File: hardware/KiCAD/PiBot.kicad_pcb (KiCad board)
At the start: 2 copper layers, 112 x 87 mm, 179 parts, among them P1 BREAKOUT, P10 BREAKOUT, P11 BREAKOUT, P12 BREAKOUT, P2 CONN_02X05, P3 I2C_EXPANSION, P4 SPI_EXPANSION, P5 Feather-Adaper, P6 BREAKOUT, P7 BREAKOUT, P8 BREAKOUT, P9 BREAKOUT, SW1 SPST, SW2 SW_SPDT, SW3 SW_SPDT, SW4 SW_SPDT, SW5 SW_SPDT, U1 DMG2302U, U10 AH3772, U11 AH3772, U12 AH3772, U13 BH1745NUC, U14 BH1745NUC, U15 L3GD20H, U16 LSM303DLHCTR, U17 N-FET, U2 MKL03ZxxVFK4, U3 N-FET, U4 TPS63060, U5 MC33926PNB, U6 MC33926PNB, U7 Motor, U8 Motor, U9 AH3772

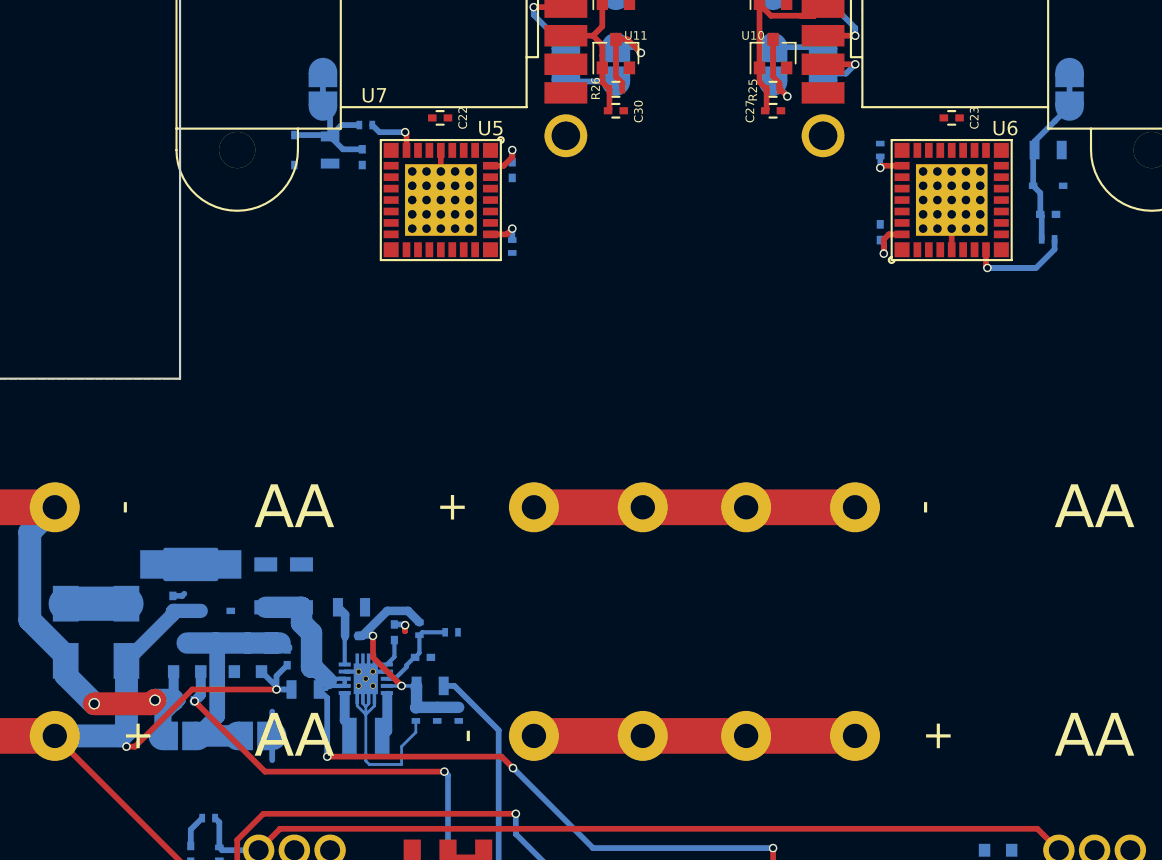
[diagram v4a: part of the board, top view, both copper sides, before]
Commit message: Wire up motor drive power
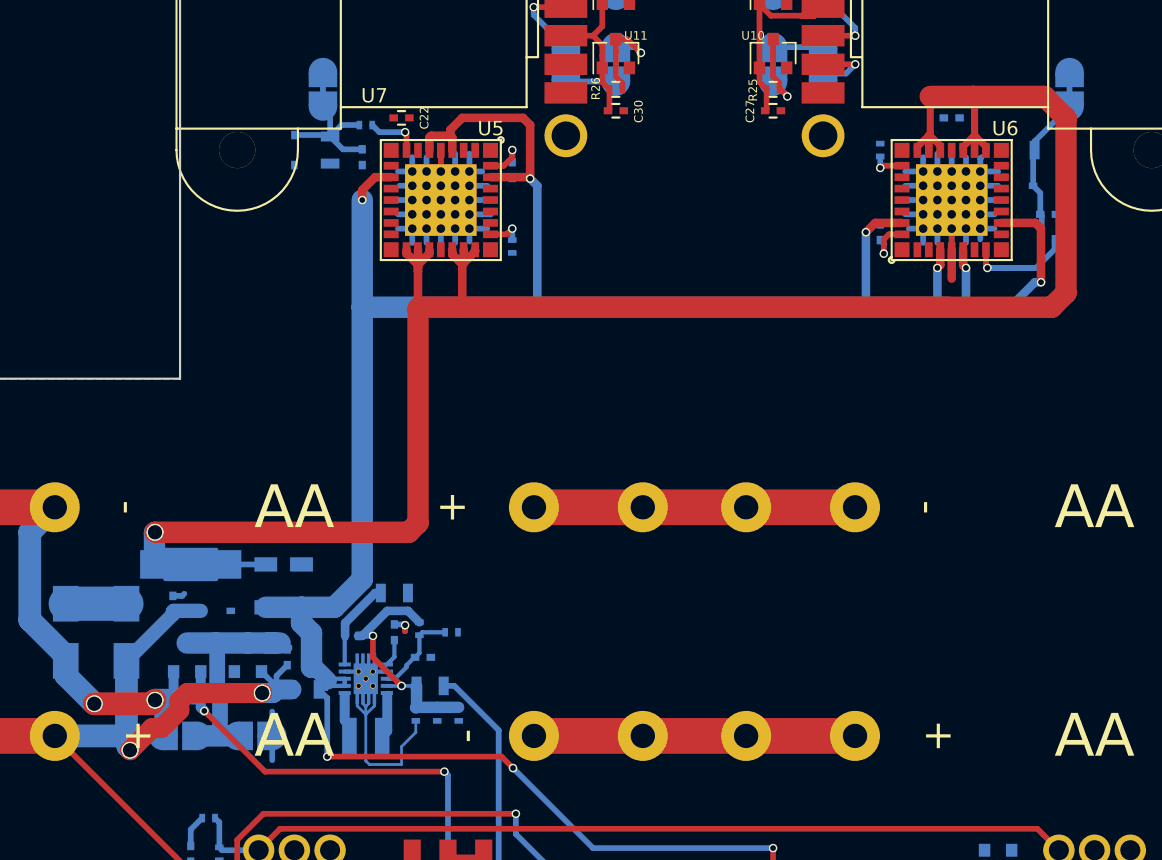
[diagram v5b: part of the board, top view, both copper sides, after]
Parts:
- C23: moved to B.Cu
- moved R12 3.16 mm to (122.0, 150.0)
- moved C22 2.70 mm to (122.5, 116.8)
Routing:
- net +BATT: track 57.2 -> 189.0 mm, vias 4 -> 10
- net GNDPWR: track 0.00 -> 131.5 mm, vias 0 -> 1
- net GND: track 25.9 -> 73.9 mm
- net Net-(R12-Pad2): track 4.22 -> 6.28 mm
- net Net-(C9-Pad2): track 17.5 -> 18.5 mm
- net /power/BATT_V+_TERM: track 78.8 -> 79.4 mm

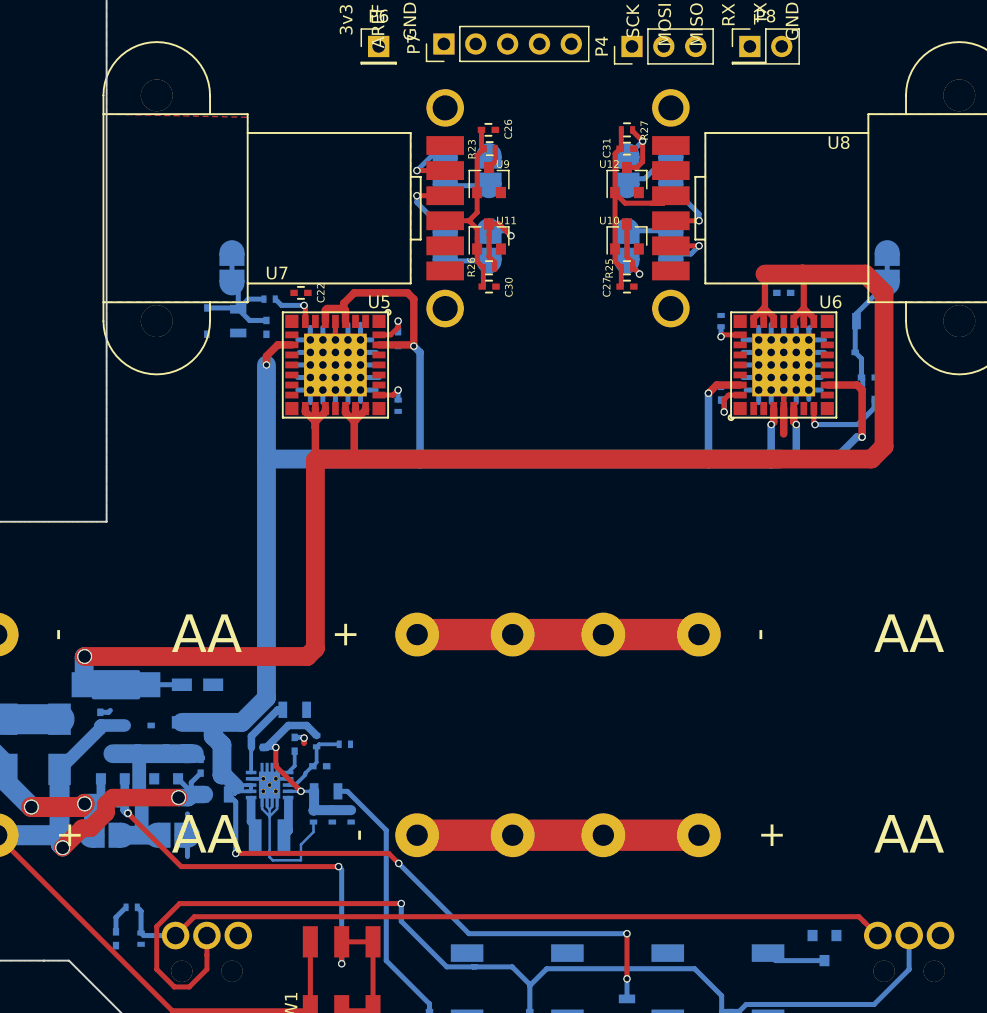
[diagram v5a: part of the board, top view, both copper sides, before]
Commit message: Motor drives wired up
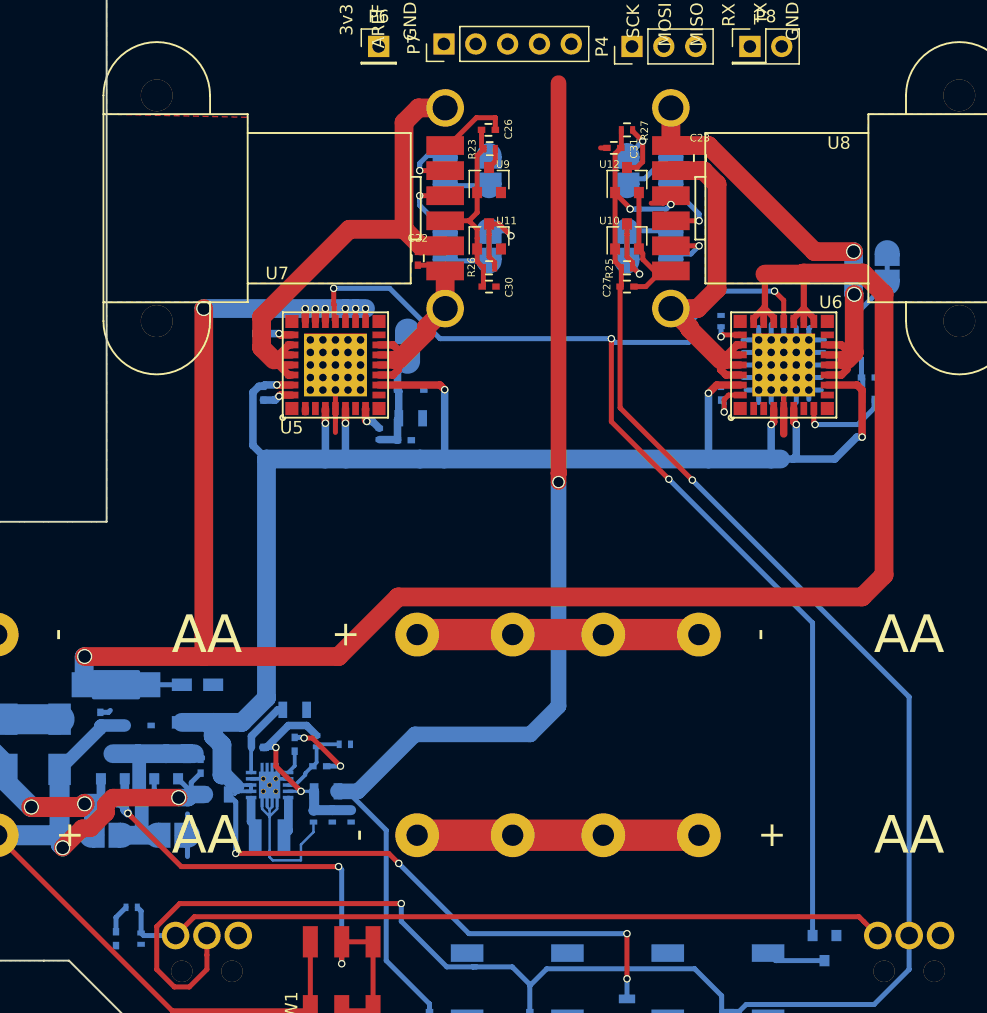
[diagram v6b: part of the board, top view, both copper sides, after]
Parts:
- C23: moved to F.Cu
- moved D11 17.2 mm to (131.2, 124.5), turned to 0 degrees
- moved R17 15.8 mm to (131.2, 126.8), turned to 0 degrees
- moved JP5 15.3 mm to (131.0, 121.0)
- moved C20 14.2 mm to (130.8, 128.5), turned to 0 degrees
- moved R19 13.9 mm to (128.8, 128.0), turned to 270 degrees
- moved C23 12.7 mm to (154.3, 106.0), turned to 270 degrees
- moved R21 12.4 mm to (119.2, 120.0), turned to 180 degrees
- moved C19 11.6 mm to (119.5, 124.8), turned to 270 degrees
- moved C22 9.72 mm to (131.8, 114.0), turned to 90 degrees
- moved C31 1.05 mm to (147.4, 105.2), turned to 180 degrees
- turned U5 to 90 degrees
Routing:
- net ~MotorSF: track 0.00 -> 99.2 mm, vias 0 -> 4
- net +5V: track 21.0 -> 91.2 mm, vias 0 -> 1
- net +3V3: track 119.3 -> 181.6 mm, vias 1 -> 4
- net Net-(C22-Pad2): track 0.00 -> 42.0 mm
- net Net-(C23-Pad1): track 0.00 -> 39.5 mm, vias 0 -> 2
- net Net-(C23-Pad2): track 0.00 -> 31.1 mm
- net GNDPWR: track 131.5 -> 162.3 mm, vias 1 -> 8
- net Net-(C22-Pad1): track 0.00 -> 19.4 mm
- net +BATT: track 189.0 -> 181.0 mm, vias 10 -> 12
- net GND: track 73.9 -> 77.5 mm, vias 1 -> 2
- net Net-(C20-Pad1): track 9.85 -> 8.18 mm
- net Net-(R19-Pad1): track 3.82 -> 2.42 mm
- net Net-(R32-Pad1): track 41.5 -> 42.2 mm
- net Net-(C19-Pad2): track 3.12 -> 2.44 mm

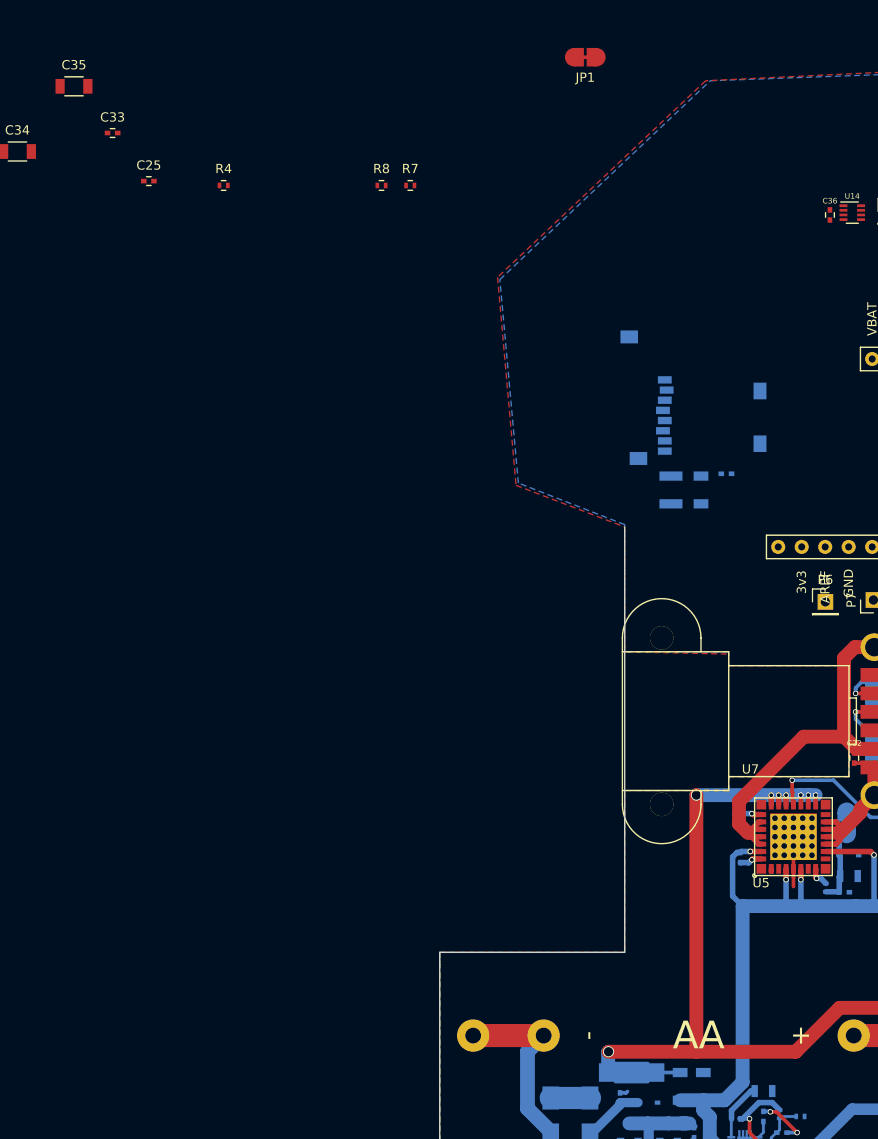
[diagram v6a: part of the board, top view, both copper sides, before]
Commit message: fixing GND_PWR connection
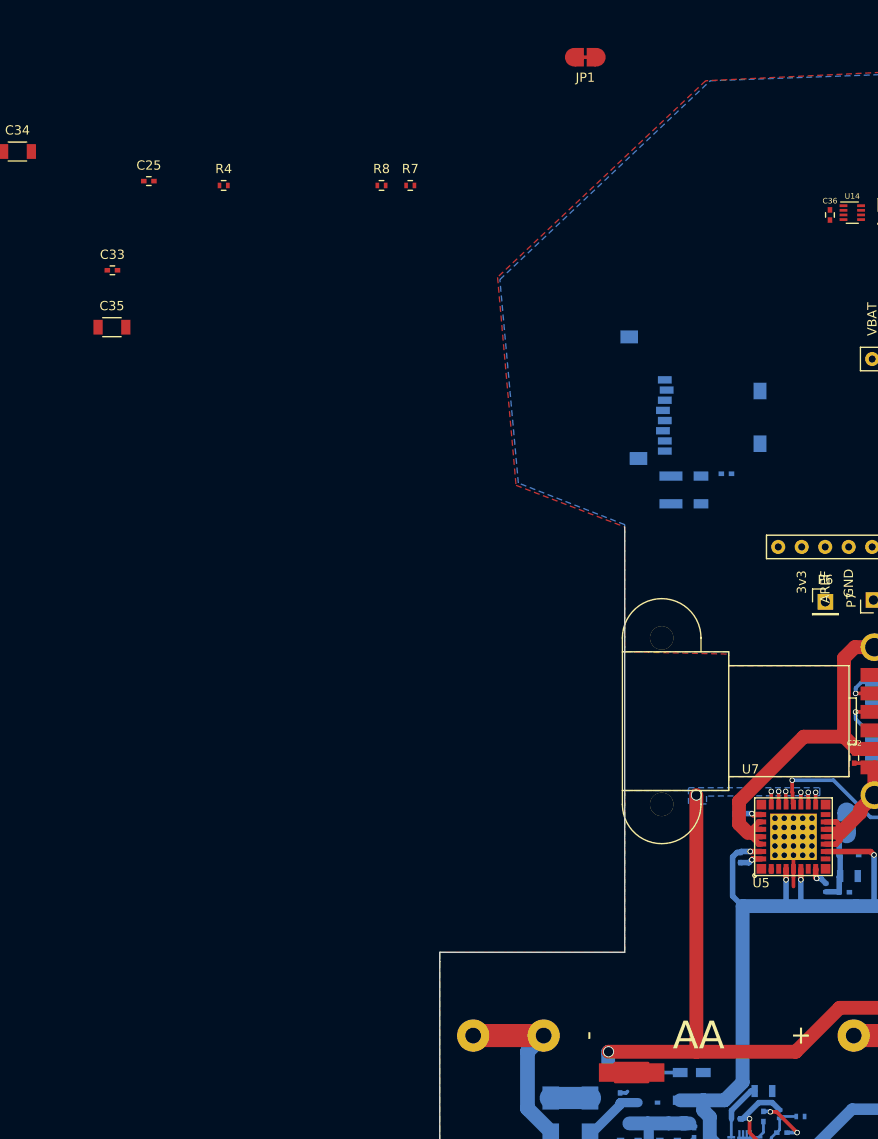
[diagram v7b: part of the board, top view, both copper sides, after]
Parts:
- JP17: moved to F.Cu
- moved C35 26.4 mm to (51.5, 67.4)
- moved C33 14.8 mm to (51.6, 61.2)
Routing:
- net GNDPWR: track 162.3 -> 150.7 mm
- added copper zone on B.Cu, net GNDPWR

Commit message: Revert "fixing GND_PWR connection" because it is not compatible with the current stable version of KiCad
This reverts commit 5be297efdf6c88a46329cd071e672a911a750ef8.
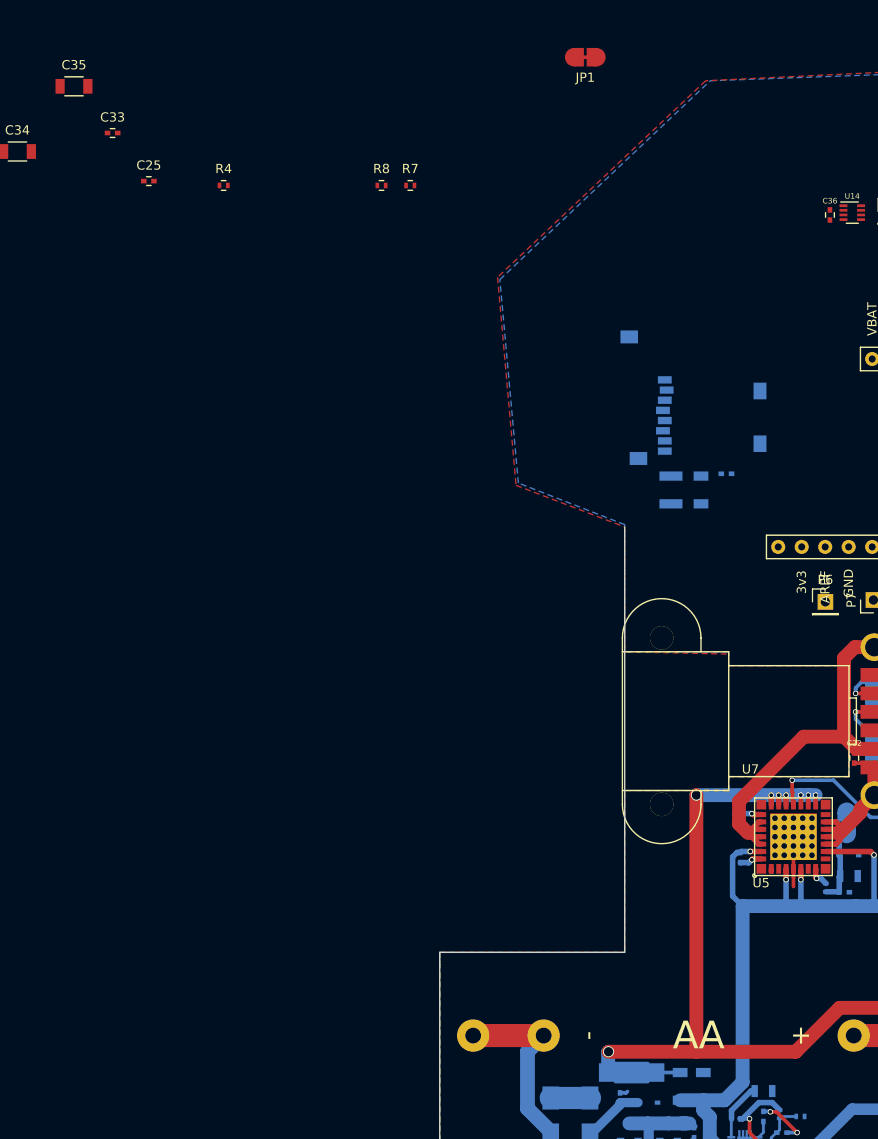
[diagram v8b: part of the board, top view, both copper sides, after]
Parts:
- JP17: moved to B.Cu
- moved C35 26.4 mm to (47.4, 41.4)
- moved C33 14.8 mm to (51.6, 46.4)
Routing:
- net GNDPWR: track 150.7 -> 162.3 mm
- removed copper zone on B.Cu, net GNDPWR
